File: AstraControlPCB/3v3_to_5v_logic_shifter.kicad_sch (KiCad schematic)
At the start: 18 parts, among them U6 TXB0104PWR

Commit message: Update schematic titles, templates
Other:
- title: AstraControl - Root -> AstraControl - 3V3 to 5V Logic Shifter
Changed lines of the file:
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@@
 	(paper "A4")
 	(title_block
-		(title "AstraControl - Root")
+		(title "AstraControl - 3V3 to 5V Logic Shifter")
 		(date "2024-08-26")
 		(rev "A")

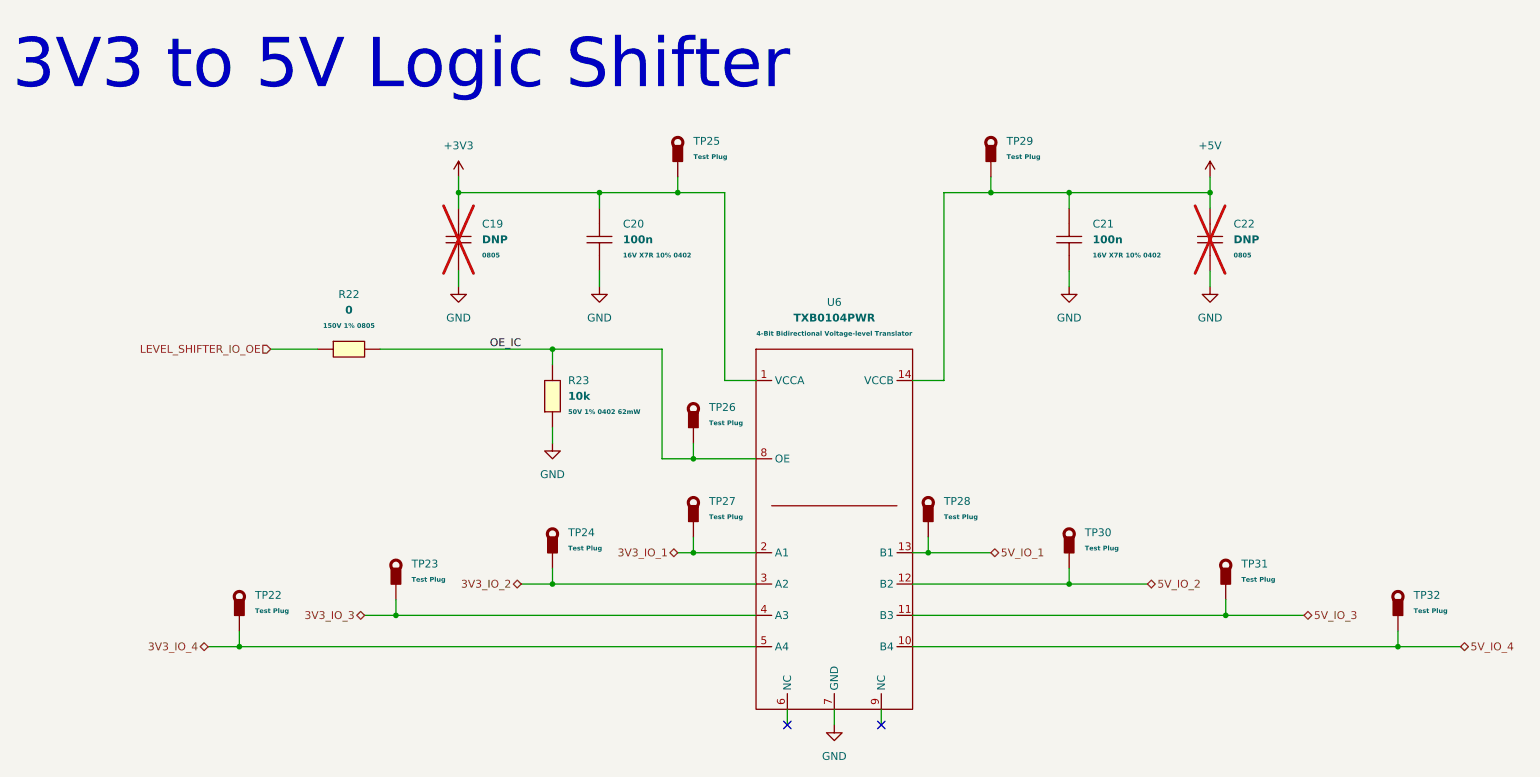
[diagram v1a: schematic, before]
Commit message: Update to new rs485 chip, use 2 bit 5v gpio
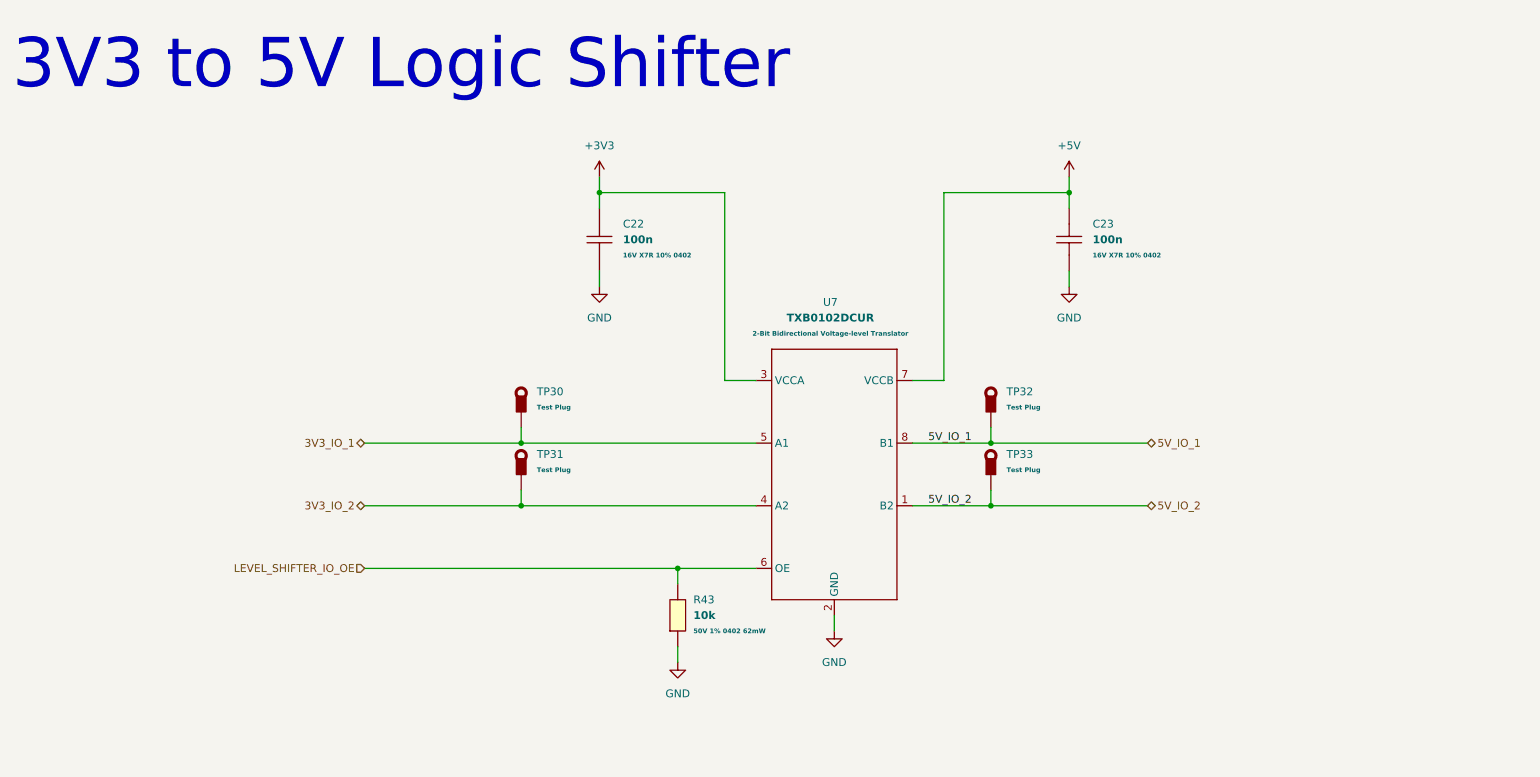
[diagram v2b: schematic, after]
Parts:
- removed C19, C22: DNP, LiveAstra:C_DNP_0805_2012Metric_Pad1.18x1.45mm_HandSolder, symbol LiveAstra:C_DNP_0805
- removed R22: 0, LiveAstra:R_0805_2012Metric_Pad1.20x1.40mm_HandSolder, symbol LiveAstra:R_0Ohm_0805_125mW
- removed TP22, TP23, TP25, TP26, TP29, TP31, TP32: TestPoint_Thimble, LiveAstra:TestPoint_Loop_D3.50mm_Drill0.9mm_Beaded, symbol LiveAstra:TestPoint_Thimble
- removed U6: TXB0104PWR, LiveAstra:LOGIC_SHIFTER_TXB0104PWR_TSOP_14, symbol LiveAstra:U_TXB0104PWR_4Bit_Logic_Level_Translator
- added U7: TXB0102DCUR, LiveAstra:U_LOGIC_SHIFTER_TXB0102DCUR_VSSOP_8, symbol LiveAstra:U_TXB0102DCUR_2Bit_Logic_Level_Translator
- renumbered C20 to C22, C21 to C23, R23 to R43, TP27 to TP30, TP24 to TP31, TP28 to TP32, TP30 to TP33
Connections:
- net OE_IC is gone; now on net LEVEL_SHIFTER_IO_OE: R43.2
- net +3V3: now also U7.3 (VCCA)
- net +5V: now also U7.7 (VCCB)
- net 3V3_IO_1: now also U7.5 (A1)
- net 3V3_IO_2: now also U7.4 (A2)
- net 5V_IO_1: now also U7.8 (B1)
- net 5V_IO_2: now also U7.1 (B2)
- net GND: now also U7.2 (GND)
- net LEVEL_SHIFTER_IO_OE: now also U7.6 (OE)
- no-connect marks 2 -> 0
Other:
- moved on the sheet: R43, TP30, TP31, TP32, TP33

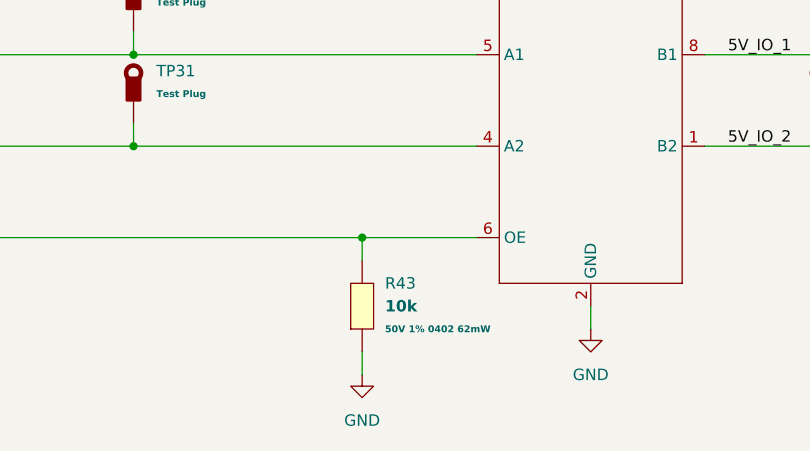
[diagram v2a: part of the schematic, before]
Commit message: New inductor that is in stock, updated rs485 ic layout to put caps closer
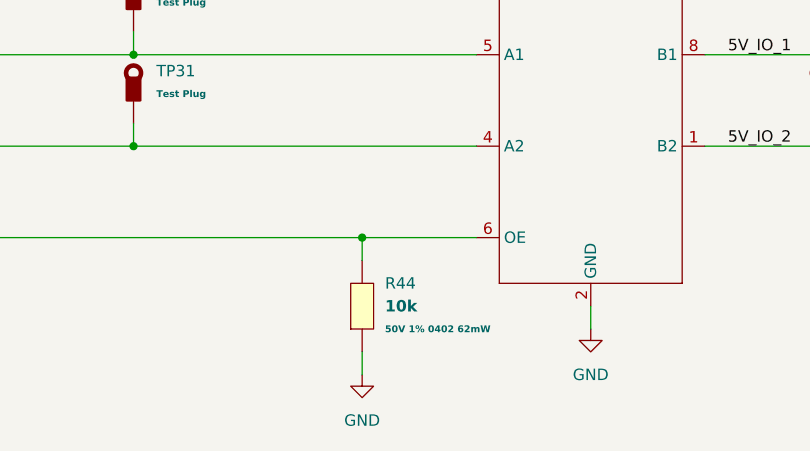
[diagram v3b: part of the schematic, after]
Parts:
- renumbered R43 to R44
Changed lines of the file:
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@@
 		(dnp no)
 		(fields_autoplaced yes)
-		(property "Reference" "#PWR080"
+		(property "Reference" "#PWR081"
 			(at 190.5 72.39 0)
 			(effects
@@
 			(project "AstraControl"
 				(path "/9a751838-dce8-4d69-8a02-736625ac74e7/0db21d8e-3390-4d67-877f-0e5d98e37848/d42b2a5d-6ce6-4b16-bfed-4946742bc91a"
-					(reference "#PWR080")
+					(reference "#PWR081")
 					(unit 1)
 				)
@@
 		(dnp no)
 		(fields_autoplaced yes)
-		(property "Reference" "R43"
+		(property "Reference" "R44"
 			(at 129.54 116.8399 90)
 			(effects
@@
 			(project "AstraControl"
 				(path "/9a751838-dce8-4d69-8a02-736625ac74e7/0db21d8e-3390-4d67-877f-0e5d98e37848/d42b2a5d-6ce6-4b16-bfed-4946742bc91a"
-					(reference "R43")
+					(reference "R44")
 					(unit 1)
 				)
@@
 		(dnp no)
 		(fields_autoplaced yes)
-		(property "Reference" "#PWR077"
+		(property "Reference" "#PWR078"
 			(at 127 133.35 0)
 			(effects
@@
 			(project "AstraControl"
 				(path "/9a751838-dce8-4d69-8a02-736625ac74e7/0db21d8e-3390-4d67-877f-0e5d98e37848/d42b2a5d-6ce6-4b16-bfed-4946742bc91a"
-					(reference "#PWR077")
+					(reference "#PWR078")
 					(unit 1)
 				)
@@
 		(dnp no)
 		(fields_autoplaced yes)
-		(property "Reference" "#PWR079"
+		(property "Reference" "#PWR080"
 			(at 190.5 52.07 0)
 			(effects
@@
 			(project "AstraControl"
 				(path "/9a751838-dce8-4d69-8a02-736625ac74e7/0db21d8e-3390-4d67-877f-0e5d98e37848/d42b2a5d-6ce6-4b16-bfed-4946742bc91a"
-					(reference "#PWR079")
+					(reference "#PWR080")
 					(unit 1)
 				)
@@
 		(dnp no)
 		(fields_autoplaced yes)
-		(property "Reference" "#PWR075"
+		(property "Reference" "#PWR076"
 			(at 114.3 52.07 0)
 			(effects
@@
 			(project "AstraControl"
 				(path "/9a751838-dce8-4d69-8a02-736625ac74e7/0db21d8e-3390-4d67-877f-0e5d98e37848/d42b2a5d-6ce6-4b16-bfed-4946742bc91a"
-					(reference "#PWR075")
+					(reference "#PWR076")
 					(unit 1)
 				)
@@
 		(dnp no)
 		(fields_autoplaced yes)
-		(property "Reference" "#PWR076"
+		(property "Reference" "#PWR077"
 			(at 114.3 72.39 0)
 			(effects
@@
 			(project "AstraControl"
 				(path "/9a751838-dce8-4d69-8a02-736625ac74e7/0db21d8e-3390-4d67-877f-0e5d98e37848/d42b2a5d-6ce6-4b16-bfed-4946742bc91a"
-					(reference "#PWR076")
+					(reference "#PWR077")
 					(unit 1)
 				)
@@
 		(dnp no)
 		(fields_autoplaced yes)
-		(property "Reference" "#PWR078"
+		(property "Reference" "#PWR079"
 			(at 152.4 128.27 0)
 			(effects
@@
 			(project "AstraControl"
 				(path "/9a751838-dce8-4d69-8a02-736625ac74e7/0db21d8e-3390-4d67-877f-0e5d98e37848/d42b2a5d-6ce6-4b16-bfed-4946742bc91a"
-					(reference "#PWR078")
-					(unit 1)
-				)
+					(reference "#PWR079")
+					(unit 1)
+				)
